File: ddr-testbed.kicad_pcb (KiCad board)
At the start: 6 copper layers, 67.6 x 30 mm, 105 parts, among them J1 ddr3-sodimm-edge, U1 MT53E256M16D1

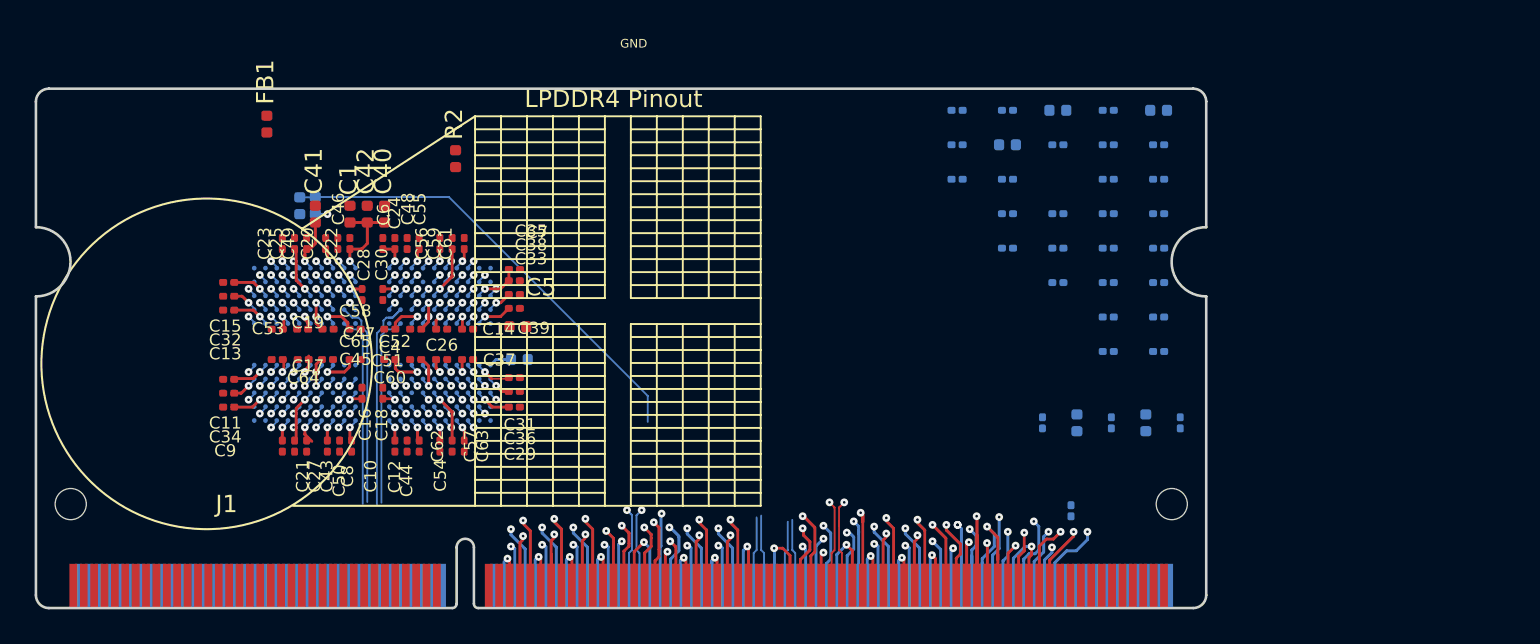
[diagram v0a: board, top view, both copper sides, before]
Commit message: Routing of all high speed DDR signals done
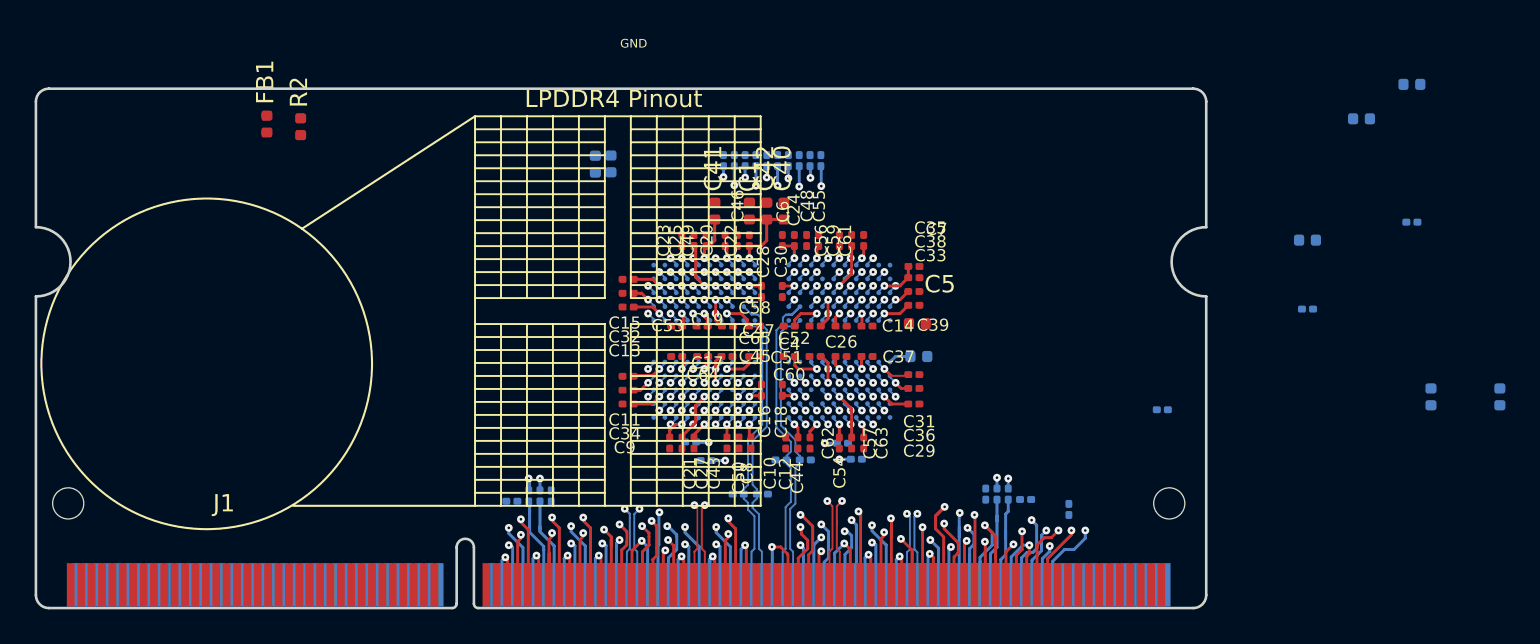
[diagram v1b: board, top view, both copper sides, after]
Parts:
- moved R33 41.2 mm to (128.6, 95.1), turned to 0 degrees
- moved R12 35.7 mm to (129.5, 94.8), turned to 270 degrees
- moved R5 33.9 mm to (130.2, 94.8), turned to 270 degrees
- moved R32 28.7 mm to (130.8, 94.8), turned to 90 degrees
- moved R20 28.6 mm to (138.9, 91.7)
- moved R21 27.3 mm to (139.8, 92.8)
- moved R24 26.5 mm to (141.4, 75.4), turned to 90 degrees
- moved R18 25.7 mm to (146.4, 75.4), turned to 90 degrees
- moved R22 23.8 mm to (142.7, 75.4), turned to 90 degrees
- moved C11 23.1 mm to (135.3, 87.9)
- moved C13 23.1 mm to (135.3, 83.9)
- moved C15 23.1 mm to (135.3, 82.3)
- moved C22 23.1 mm to (142.3, 80.0)
- moved C29 23.1 mm to (151.8, 89.5)
- moved C31 23.1 mm to (151.8, 87.8)
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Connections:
- J1 pad 84: /CKE0_B -> /CKE_1
- R11 pad 1: /CKE_0_A -> /CKE0_A
- R12 pad 1: /CKE_0_B -> /CKE0_B
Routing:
- net /RESET_CONN_N: track 31.5 -> 4.15 mm
- net /CKE0_A: track 13.9 -> 32.0 mm, vias 1 -> 3
- net /CA2_A: track 20.4 -> 35.1 mm, vias 2 -> 3
- net /CKE0_B: track 20.9 -> 35.3 mm, vias 2 -> 3
- net /CA2_B: track 21.5 -> 35.6 mm, vias 2 -> 3
- net /CA3_A: track 21.8 -> 35.8 mm, vias 2 -> 3
- net /CA4_A: track 22.3 -> 35.9 mm, vias 2 -> 3
- net /CA4_B: track 23.2 -> 36.8 mm, vias 2 -> 3
- net /CA3_B: track 24.0 -> 37.5 mm, vias 2 -> 3
- net /CA5_B: track 24.2 -> 36.8 mm, vias 2 -> 3
- net /CA5_A: track 23.8 -> 36.1 mm, vias 2 -> 3
- net /CA1_B: track 19.7 -> 31.3 mm, vias 2 -> 3
- net /CA1_A: track 17.0 -> 28.4 mm, vias 2 -> 3
- net /CA0_B: track 15.5 -> 24.2 mm, vias 2 -> 3
- net /CA0_A: track 18.5 -> 26.3 mm, vias 2 -> 3
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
